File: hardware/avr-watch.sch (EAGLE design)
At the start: 43 parts, among them IC1 MEGA48/88/168-AU, Q5 32k, U1 MAX1555

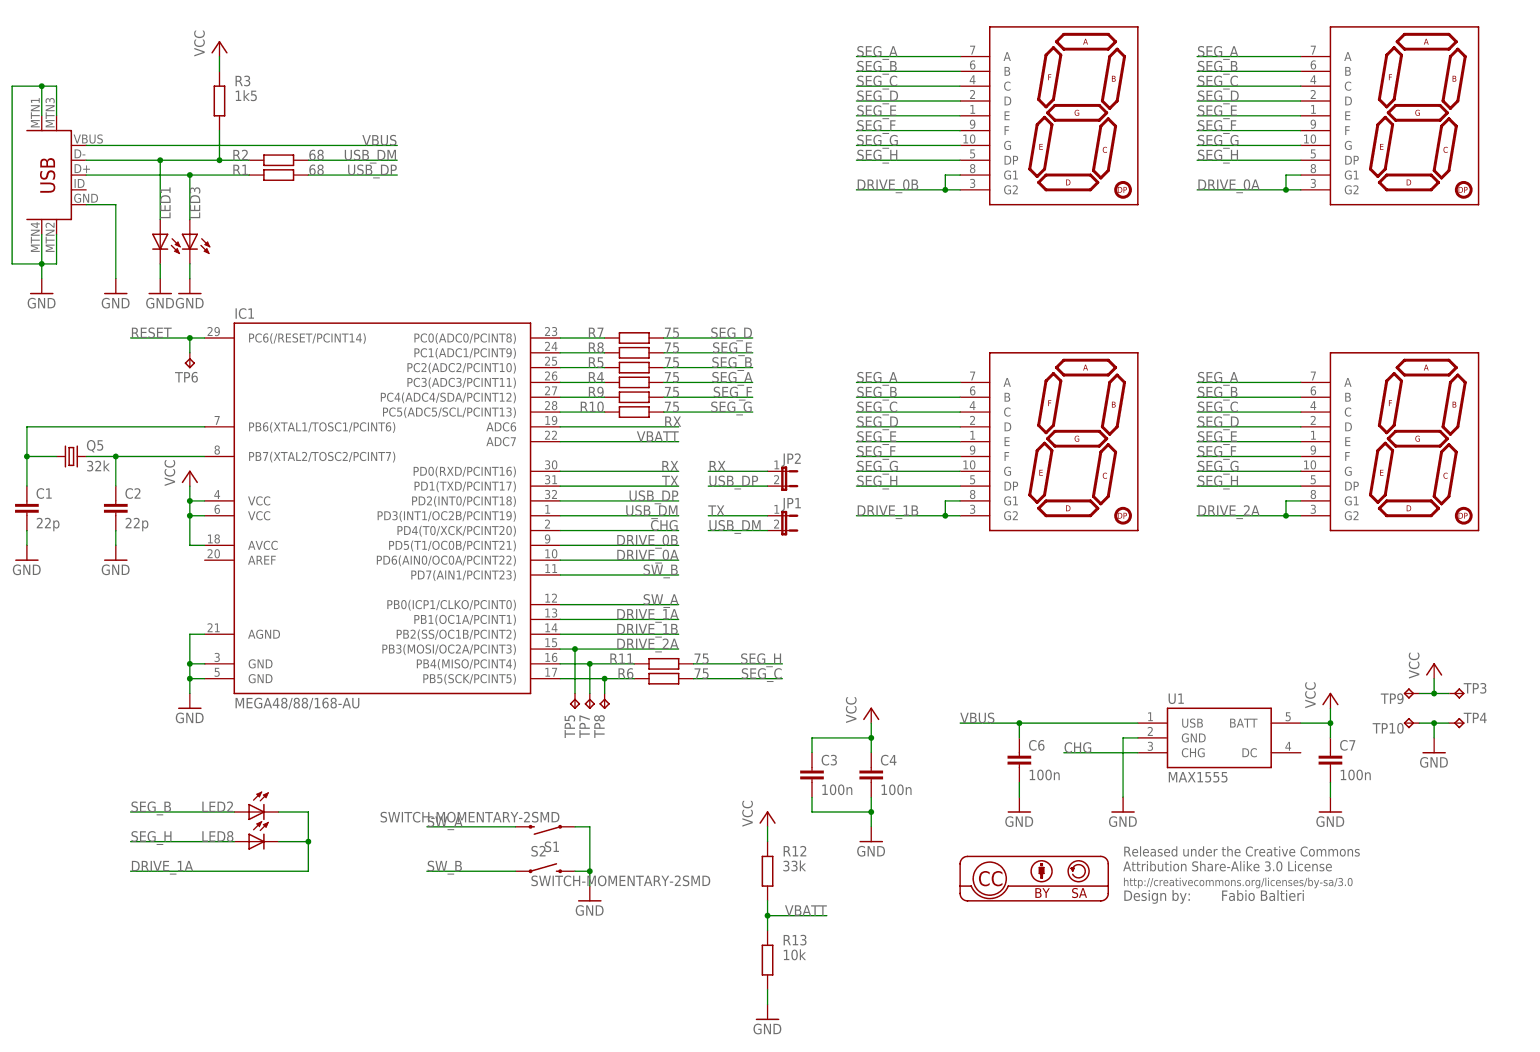
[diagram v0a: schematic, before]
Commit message: hardware: cosmetic changes, add pdf
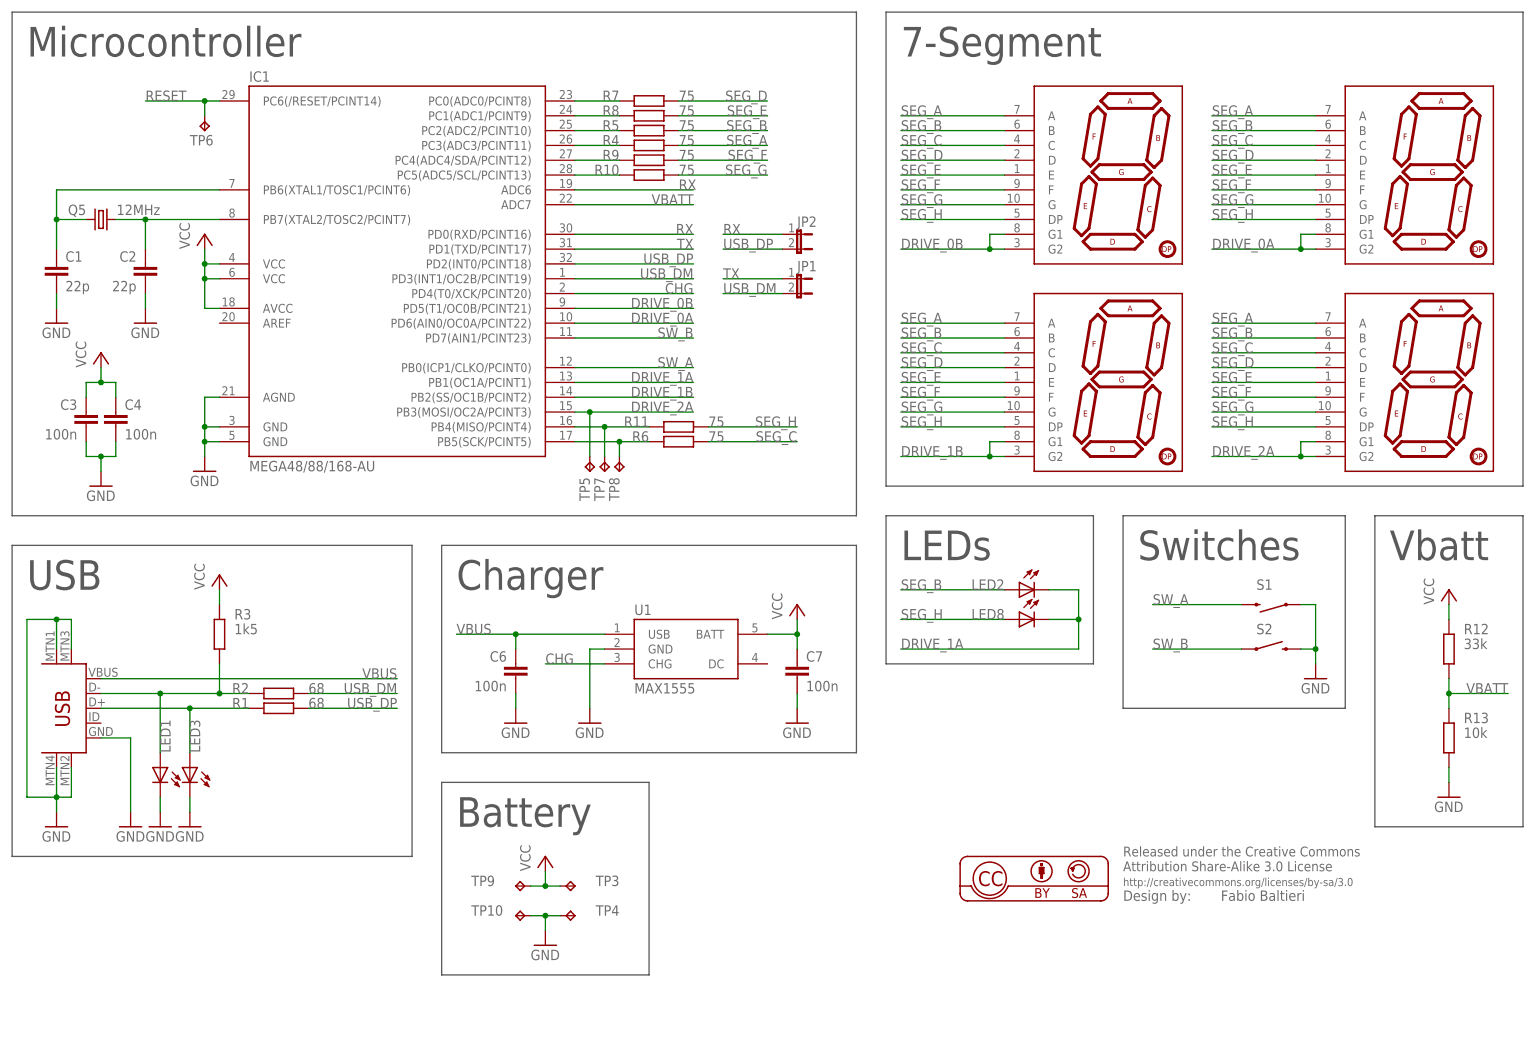
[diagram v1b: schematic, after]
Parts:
- Q5: value 32k -> 12MHz
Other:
- note added: "7-Segment"
- note added: "Battery"
- note added: "Charger"
- note added: "LEDs"
- note added: "Microcontroller"
- note added: "Switches"
- note added: "USB"
- note added: "Vbatt"
- moved on the sheet: C1, C2, C3, C4, C6, C7, IC1, JP1, JP2, LED1, LED2, LED3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
